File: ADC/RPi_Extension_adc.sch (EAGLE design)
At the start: 39 parts, among them U1 74AHC1G04GW/T1, U2 ADR423ARZ, U3 AD7616BSTZ

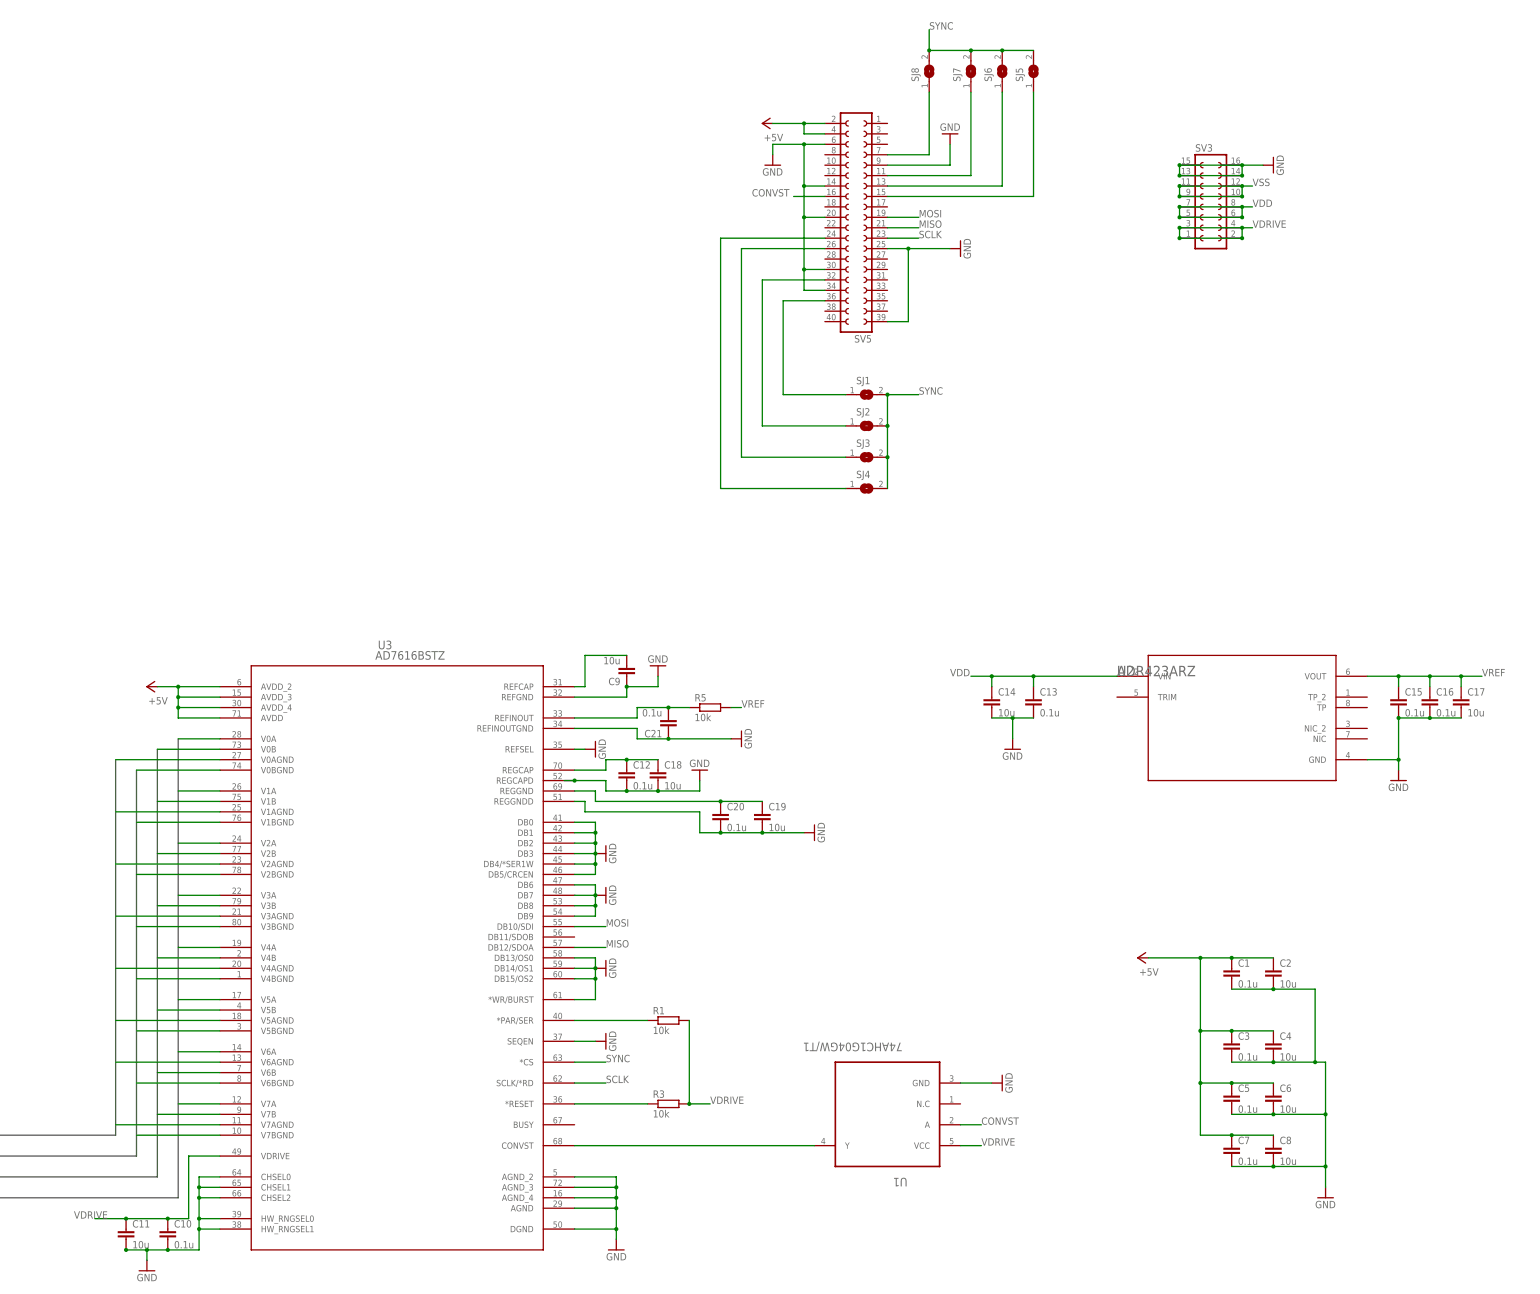
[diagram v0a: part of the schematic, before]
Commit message: used consistent naming and units for values
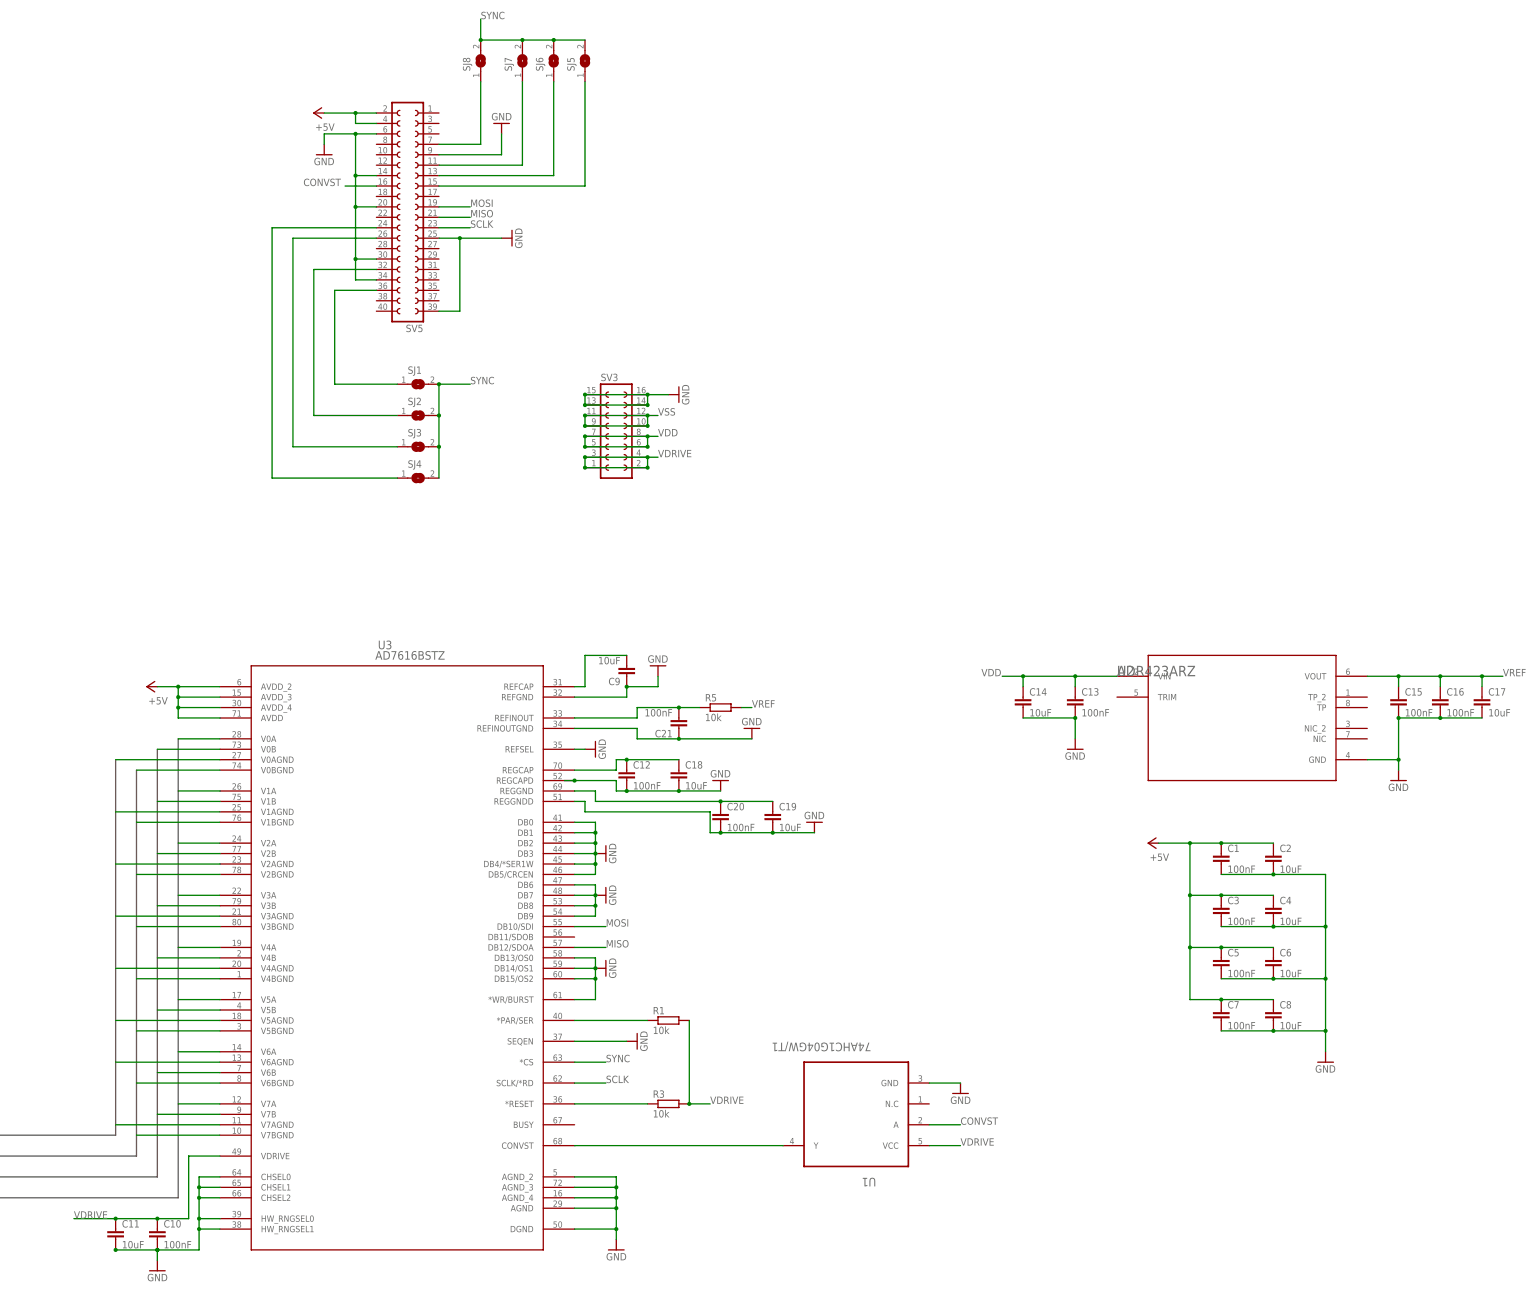
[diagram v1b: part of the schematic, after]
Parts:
- C1, C10, C12, C13, C15, C16, C20, C21, C3, C5, C7: value 0.1u -> 100nF
- C11, C14, C17, C18, C19, C2, C4, C6, C8, C9: value 10u -> 10uF
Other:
- moved on the sheet: C1, C10, C11, C13, C14, C16, C17, C18, C19, C2, C21, C3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

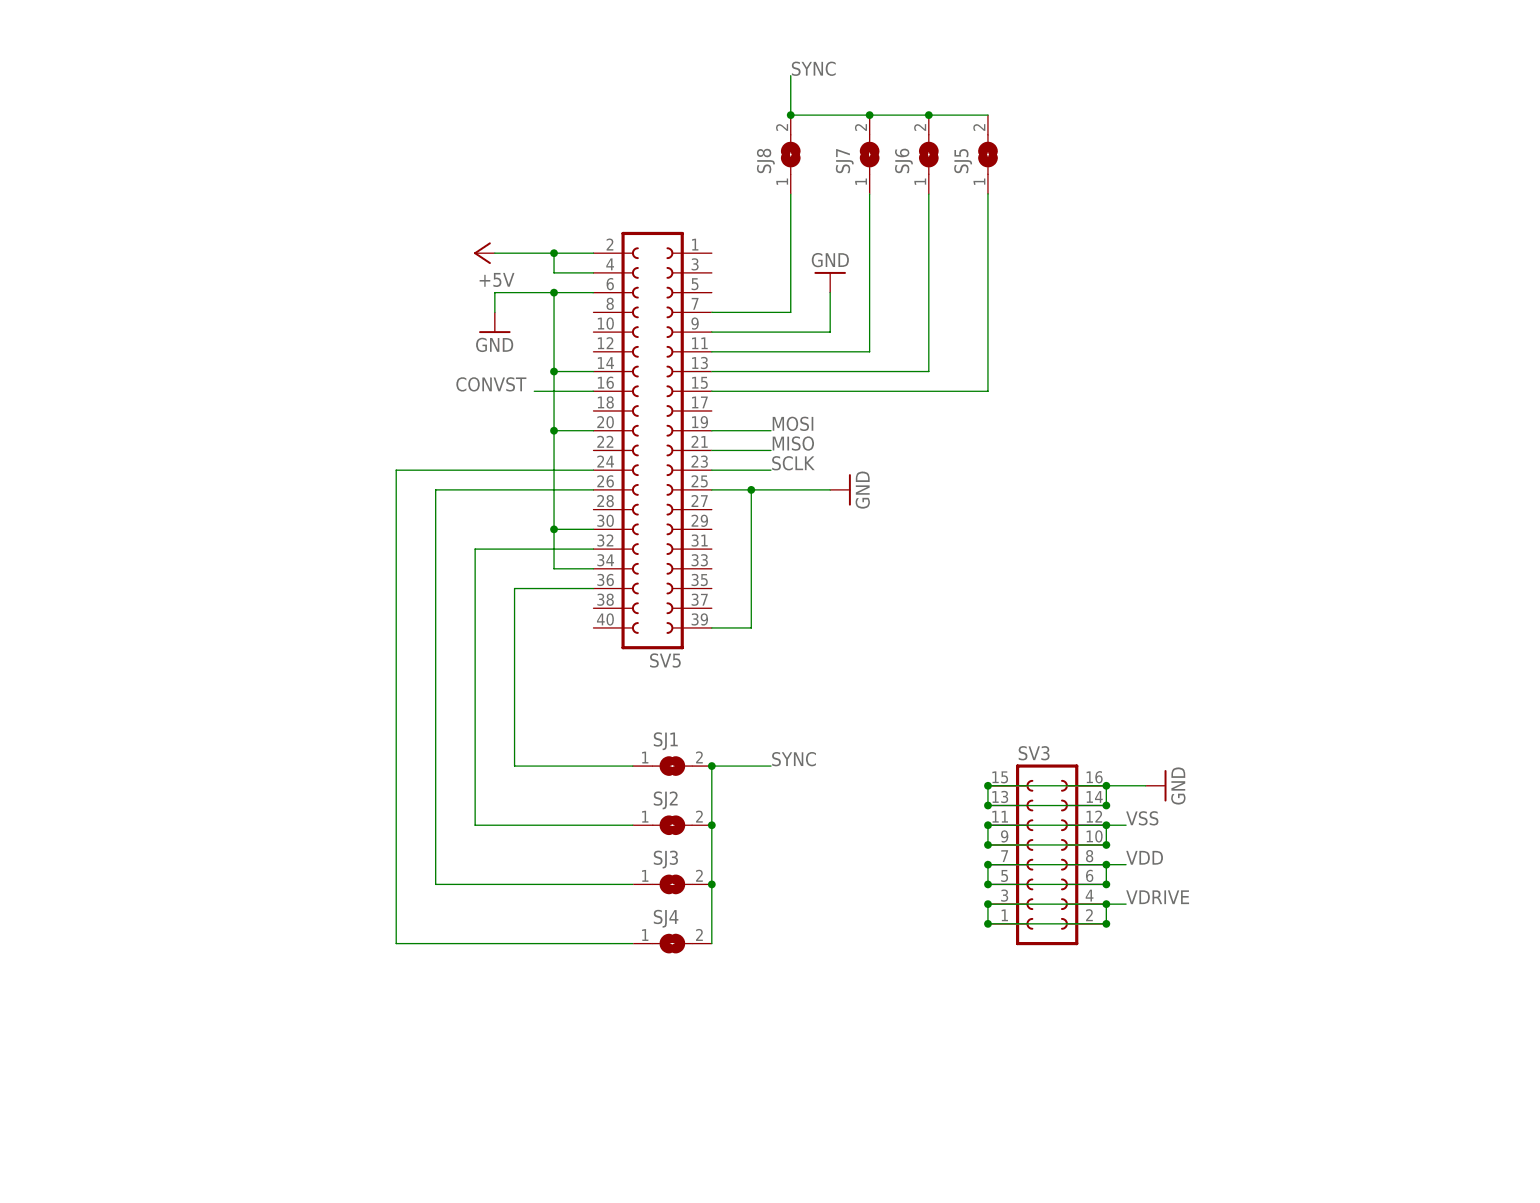
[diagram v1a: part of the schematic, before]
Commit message: added additional id jumpers to adc and dac board
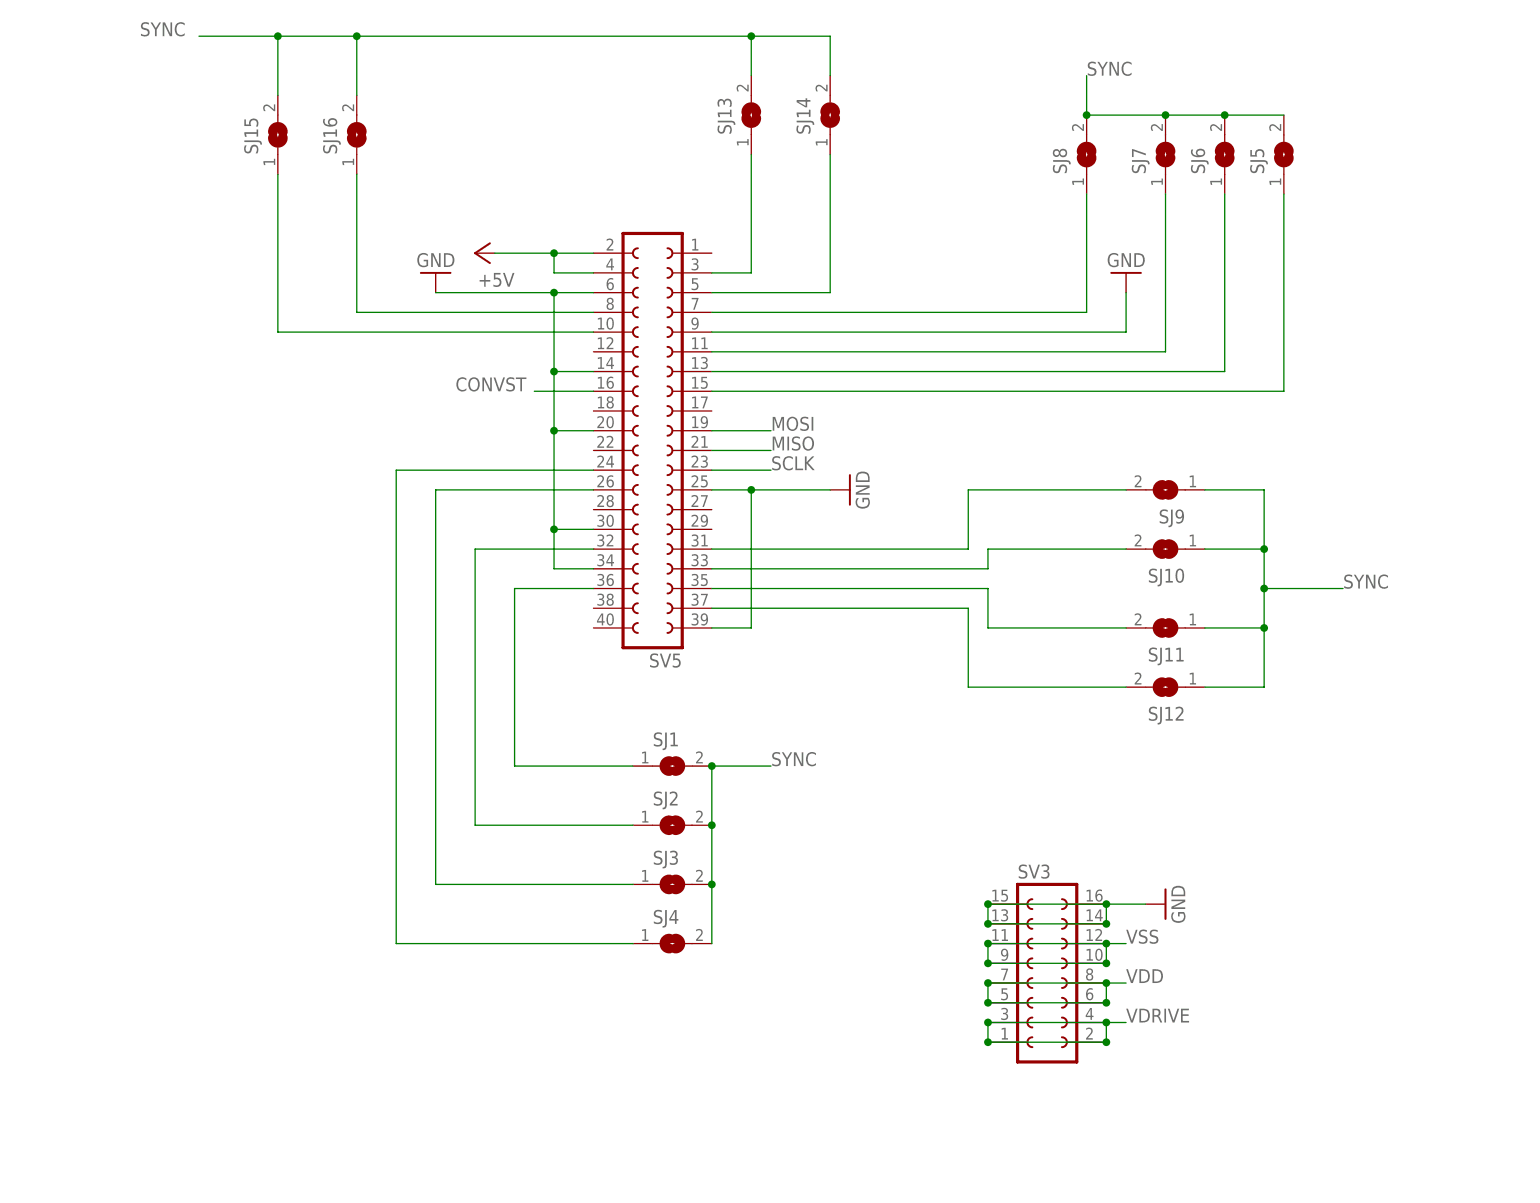
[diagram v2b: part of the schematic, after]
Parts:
- added SJ10, SJ11, SJ12, SJ13, SJ14, SJ15, SJ16, SJ9: (no value), jumper:SJ
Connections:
- new net N$11: SJ15.1, SV5.10
- new net N$12: SJ9.2, SV5.31
- new net N$13: SJ10.2, SV5.33
- new net N$14: SJ11.2, SV5.35
- new net N$15: SJ12.2, SV5.37
- new net N$5: SJ13.1, SV5.3
- new net N$8: SJ14.1, SV5.5
- new net N$9: SJ16.1, SV5.8
- net SYNC: now also SJ10.1, SJ11.1, SJ12.1, SJ13.2, SJ14.2, SJ15.2, SJ16.2, SJ9.1
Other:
- moved on the sheet: SJ5, SJ6, SJ7, SJ8, SV3

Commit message: fixed severe bug on adc board
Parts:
- renumbered SJ1 to ID3, SJ10 to ID9, SJ11 to ID10, SJ12 to ID11, SJ13 to ID12, SJ14 to ID13, SJ15 to ID15, SJ16 to ID14, SJ2 to ID2, SJ3 to ID1, SJ4 to ID0, SJ5 to ID7, SJ6 to ID6, SJ7 to ID5, SJ8 to ID4, SJ9 to ID8
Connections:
- removed net N$1 (its old number): C19.1, C20.1, U3.REGGND
- new net N$16: C19.1, C20.1, U3.REGCAPD
- net GND: now also U3.REGGND; no longer U3.REGCAPD
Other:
- moved on the sheet: C12, C18

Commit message: updated content before making repository public
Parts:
- added S1: (no value), switch-omron:10-XX
- U2: value ADR423ARZ -> ADR421ARZ
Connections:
- net GND: now also S1.P, S1.P1
- net N$7: now also S1.S
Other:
- moved on the sheet: U1
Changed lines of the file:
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@@
 <?xml version="1.0" encoding="utf-8"?>
 <!DOCTYPE eagle SYSTEM "eagle.dtd">
-<eagle version="7.6.0">
+<eagle version="8.1.0">
 <drawing>
 <settings>
@@
 <part name="ID1" library="jumper" deviceset="SJ" device=""/>
 <part name="ID0" library="jumper" deviceset="SJ" device=""/>
-<part name="U2" library="ADR423ARZ" deviceset="ADR423ARZ" device=""/>
+<part name="U2" library="ADR423ARZ" deviceset="ADR423ARZ" device="" value="ADR421ARZ"/>
 <part name="GND7" library="supply1" deviceset="GND" device=""/>
 <part name="C13" library="rcl" deviceset="C-EU" device="C0603" value="100nF"/>
@@
 <part name="GND20" library="supply1" deviceset="GND" device=""/>
 <part name="GND21" library="supply1" deviceset="GND" device=""/>
+<part name="S1" library="switch-omron" deviceset="10-XX" device=""/>
 </parts>
 <sheets>
@@
 <instance part="GND17" gate="1" x="269.24" y="160.02" rot="MR180"/>
 <instance part="GND18" gate="1" x="246.38" y="175.26" rot="MR180"/>
-<instance part="U1" gate="A" x="294.64" y="63.5" rot="R180"/>
-<instance part="GND19" gate="1" x="320.04" y="71.12" rot="MR0"/>
+<instance part="U1" gate="A" x="287.02" y="30.48" rot="R180"/>
+<instance part="GND19" gate="1" x="314.96" y="50.8" rot="MR270"/>
 <instance part="ID8" gate="1" x="251.46" y="279.4" rot="R180"/>
 <instance part="ID9" gate="1" x="251.46" y="271.78" rot="R180"/>
@@
 <instance part="GND20" gate="1" x="241.3" y="134.62" rot="MR0"/>
 <instance part="GND21" gate="1" x="248.92" y="134.62" rot="MR0"/>
+<instance part="S1" gate="1" x="294.64" y="63.5" rot="R90"/>
 </instances>
 <busses>
@@
 <pinref part="U1" gate="A" pin="GND"/>
 <pinref part="GND19" gate="1" pin="GND"/>
-<wire x1="312.42" y1="73.66" x2="320.04" y2="73.66" width="0.1524" layer="91"/>
+<wire x1="312.42" y1="50.8" x2="312.42" y2="40.64" width="0.1524" layer="91"/>
+<junction x="312.42" y="50.8"/>
+<wire x1="312.42" y1="40.64" x2="304.8" y2="40.64" width="0.1524" layer="91"/>
+<pinref part="S1" gate="1" pin="P"/>
+<wire x1="299.72" y1="63.5" x2="302.26" y2="63.5" width="0.1524" layer="91"/>
+<wire x1="302.26" y1="63.5" x2="312.42" y2="63.5" width="0.1524" layer="91"/>
+<wire x1="312.42" y1="63.5" x2="312.42" y2="50.8" width="0.1524" layer="91"/>
+<pinref part="S1" gate="1" pin="P1"/>
+<wire x1="299.72" y1="66.04" x2="302.26" y2="66.04" width="0.1524" layer="91"/>
+<wire x1="302.26" y1="66.04" x2="302.26" y2="63.5" width="0.1524" layer="91"/>
+<junction x="302.26" y="63.5"/>
 </segment>
 <segment>
@@
 <segment>
 <pinref part="U1" gate="A" pin="VCC"/>
-<wire x1="312.42" y1="58.42" x2="320.04" y2="58.42" width="0.1524" layer="91"/>
-<label x="320.04" y="58.42" size="1.778" layer="95"/>
+<wire x1="304.8" y1="25.4" x2="312.42" y2="25.4" width="0.1524" layer="91"/>
+<label x="312.42" y="25.4" size="1.778" layer="95"/>
 </segment>
 </net>
@@
 <segment>
 <pinref part="U1" gate="A" pin="A"/>
-<wire x1="312.42" y1="63.5" x2="320.04" y2="63.5" width="0.1524" layer="91"/>
-<label x="320.04" y="63.5" size="1.778" layer="95"/>
+<wire x1="304.8" y1="30.48" x2="312.42" y2="30.48" width="0.1524" layer="91"/>
+<label x="312.42" y="30.48" size="1.778" layer="95"/>
 </segment>
 <segment>
@@
 <pinref part="R3" gate="G$1" pin="1"/>
 <wire x1="226.06" y1="68.58" x2="243.84" y2="68.58" width="0.1524" layer="91"/>
+<wire x1="243.84" y1="68.58" x2="243.84" y2="63.5" width="0.1524" layer="91"/>
+<junction x="243.84" y="68.58"/>
+<pinref part="S1" gate="1" pin="S"/>
+<wire x1="243.84" y1="63.5" x2="289.56" y2="63.5" width="0.1524" layer="91"/>
 </segment>
 </net>
@@
 <pinref part="U3" gate="A" pin="CONVST"/>
 <pinref part="U1" gate="A" pin="Y"/>
-<wire x1="226.06" y1="58.42" x2="276.86" y2="58.42" width="0.1524" layer="91"/>
-</segment>
-</net>
+<wire x1="226.06" y1="58.42" x2="269.24" y2="58.42" width="0.1524" layer="91"/>
+<wire x1="269.24" y1="58.42" x2="269.24" y2="25.4" width="0.1524" layer="91"/>
+</segment>
+</net>

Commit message: updated reference voltage on dac board
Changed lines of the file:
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@@
 <?xml version="1.0" encoding="utf-8"?>
 <!DOCTYPE eagle SYSTEM "eagle.dtd">
-<eagle version="8.1.0">
+<eagle version="8.4.3">
 <drawing>
 <settings>
 <setting alwaysvectorfont="no"/>
+<setting keepoldvectorfont="yes"/>
 <setting verticaltext="up"/>
 </settings>
@@
 <instance part="ID1" gate="1" x="187.96" y="228.6"/>
 <instance part="ID0" gate="1" x="187.96" y="220.98"/>
-<instance part="U2" gate="A" x="358.14" y="172.72"/>
+<instance part="U2" gate="A" x="358.14" y="172.72" smashed="yes">
+<attribute name="NAME" x="358.14" y="172.72" size="2.54" layer="95" ratio="10" rot="SR0"/>
+<attribute name="VALUE" x="368.3" y="149.86" size="2.54" layer="96" ratio="10" rot="SR0"/>
+</instance>
 <instance part="GND7" gate="1" x="347.98" y="154.94"/>
 <instance part="C13" gate="G$1" x="347.98" y="167.64"/>
